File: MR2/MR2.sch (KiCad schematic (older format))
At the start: 12 parts, among them J1 Conn_01x04_Male, J2 Conn_01x04_Male, J3 Conn_01x04_Male, J4 Conn_01x04_Male, J5 Conn_01x02_Male, J6 Conn_01x02_Male, J7 Conn_01x04_Male, J8 Conn_01x02_Male, J9 Conn_01x02_Male, U5 LPC1768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

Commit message: update:MR2の基板完成
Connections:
- net IO_1A: now also J2.2 (Pin_2); no longer J2.3 (Pin_3)
- net IO_1B: now also J2.3 (Pin_3); no longer J2.2 (Pin_2)
- net enc_collect_a: now also J3.2 (Pin_2); no longer J3.3 (Pin_3)
- net enc_collect_b: now also J3.3 (Pin_3); no longer J3.2 (Pin_2)
- net sw1: now also U5.7 (p7)
- net sw2: now also U5.8 (p8)
- net sw3: now also U5.9 (p9)
- no-connect marks 17 -> 23
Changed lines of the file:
@@
 Text GLabel 4300 3200 2    50   Input ~ 0
 PWM_1
+Text GLabel 4300 3400 2    50   Input ~ 0
+IO_1B
 Text GLabel 4300 3300 2    50   Input ~ 0
-IO_1B
-Text GLabel 4300 3400 2    50   Input ~ 0
 IO_1A
 Wire Wire Line
@@
 Text GLabel 5900 2350 2    50   Input ~ 0
 enc_elevator_a
+Text GLabel 5900 3000 2    50   Input ~ 0
+enc_collect_b
 Text GLabel 5900 2900 2    50   Input ~ 0
-enc_collect_b
-Text GLabel 5900 3000 2    50   Input ~ 0
 enc_collect_a
 Wire Notes Line
@@
 	1    0    0    -1
 $EndComp
-NoConn ~ 5300 4300
 Text Label 3350 4850 0    50   ~ 0
 motor
 Text Label 6700 5700 0    50   ~ 0
 switch
+NoConn ~ 5300 4600
+NoConn ~ 5300 4700
+NoConn ~ 5300 4800
+NoConn ~ 5300 4900
+NoConn ~ 6100 5100
+NoConn ~ 6100 5200
+NoConn ~ 4400 2300
+Text GLabel 5300 4300 0    50   Input ~ 0
+sw1
+Text GLabel 5300 4400 0    50   Input ~ 0
+sw2
+Text GLabel 5300 4500 0    50   Input ~ 0
+sw3
 $EndSCHEMATC

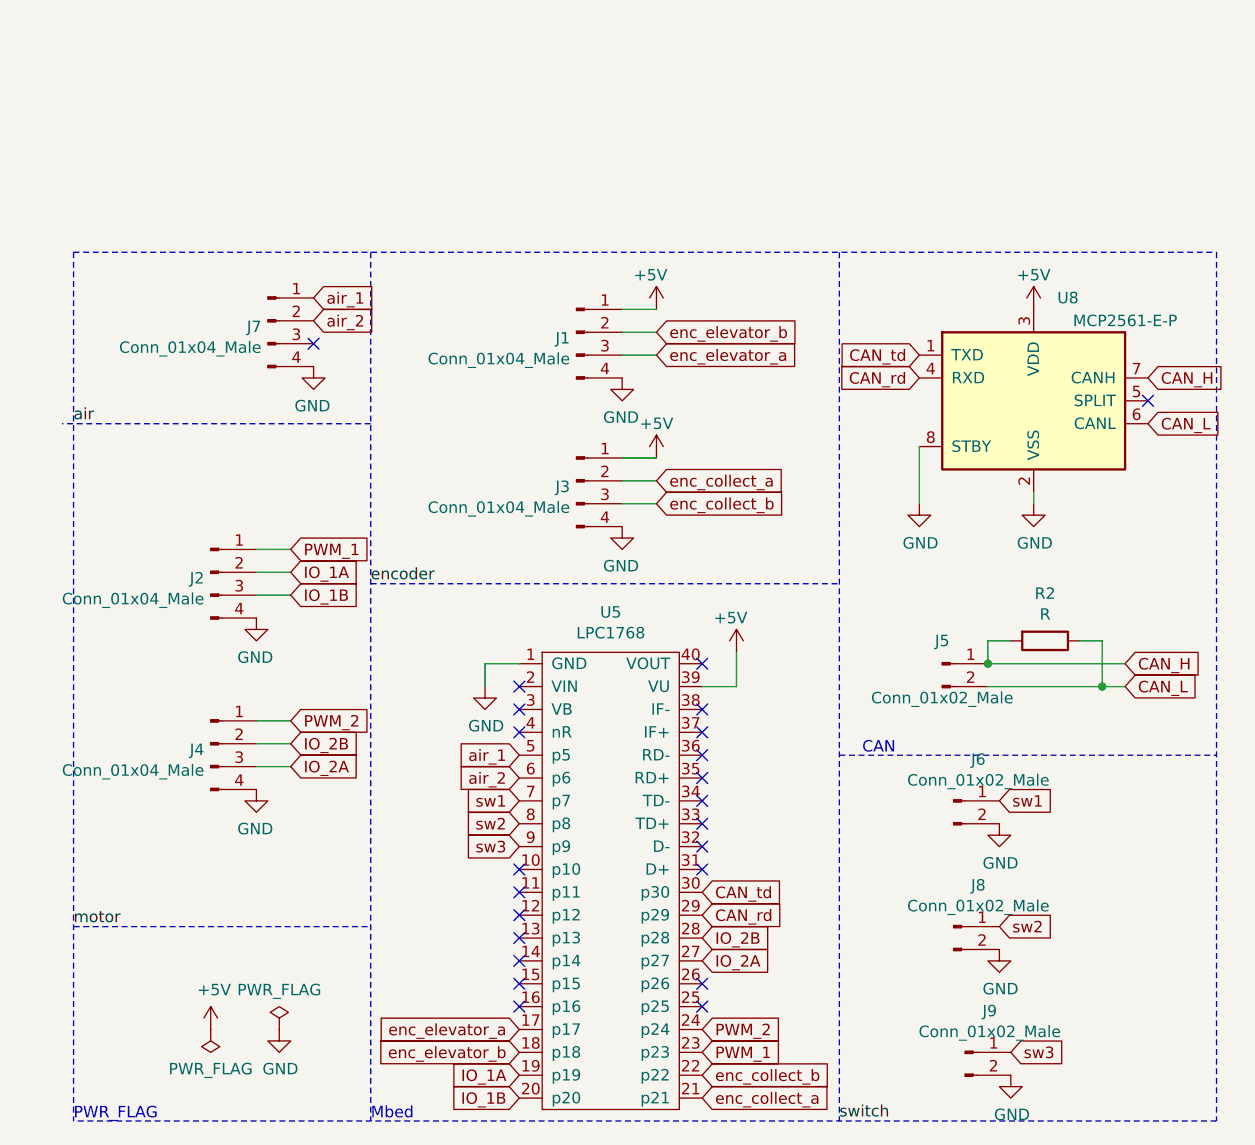
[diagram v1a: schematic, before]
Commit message: update:設計変更に伴う改修、CAN通信周りの不具合を修正
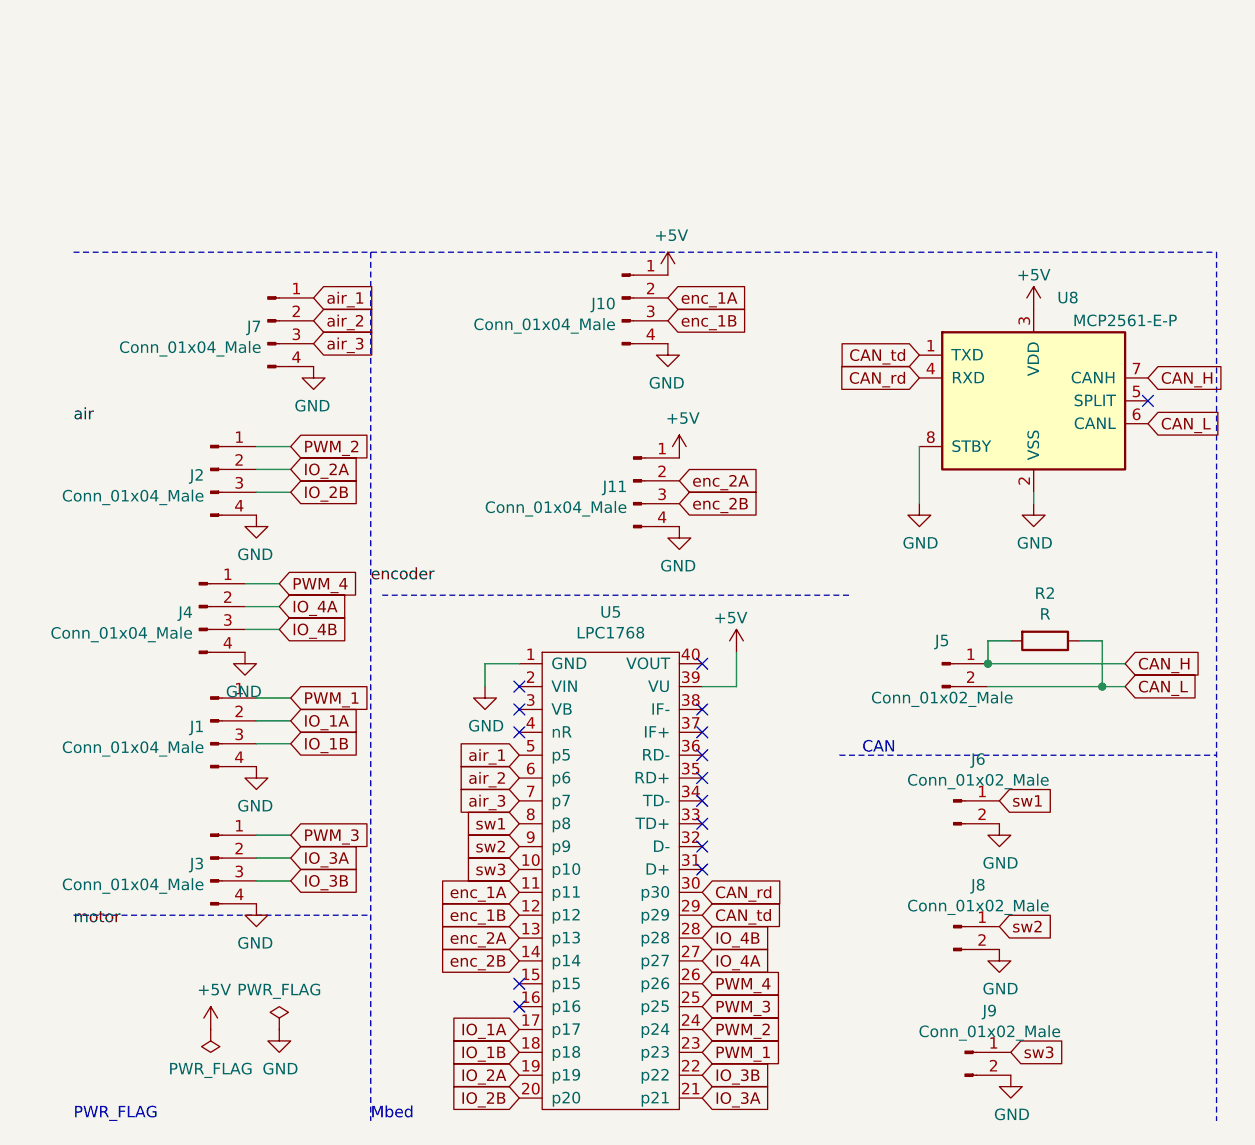
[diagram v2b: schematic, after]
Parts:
- added J10, J11: Conn_01x04_Male, Connector_JST:JST_XH_S4B-XH-A_1x04_P2.50mm_Horizontal, symbol Connector:Conn_01x04_Male
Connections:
- net +5V: now also J10.1 (Pin_1), J11.1 (Pin_1); no longer J1.1 (Pin_1), J3.1 (Pin_1)
- net CAN_rd: now also U5.30 (p30); no longer U5.29 (p29)
- net CAN_td: now also U5.29 (p29); no longer U5.30 (p30)
- net GND: now also J10.4 (Pin_4), J11.4 (Pin_4)
- net IO_1A: now also J1.2 (Pin_2), U5.17 (p17); no longer J2.2 (Pin_2), U5.19 (p19)
- net IO_1B: now also J1.3 (Pin_3), U5.18 (p18); no longer J2.3 (Pin_3), U5.20 (p20)
- net IO_2A: now also J2.2 (Pin_2), U5.19 (p19); no longer J4.3 (Pin_3), U5.27 (p27)
- net IO_2B: now also J2.3 (Pin_3), U5.20 (p20); no longer J4.2 (Pin_2), U5.28 (p28)
- net PWM_1: now also J1.1 (Pin_1); no longer J2.1 (Pin_1)
- net PWM_2: now also J2.1 (Pin_1); no longer J4.1 (Pin_1)
- net sw1: now also U5.8 (p8); no longer U5.7 (p7)
- net sw2: now also U5.9 (p9); no longer U5.8 (p8)
- net sw3: now also U5.10 (p10); no longer U5.9 (p9)
- net enc_1A: now reaches U5.11 (p11)
- net enc_1A: now also J10.2 (Pin_2)
- net enc_1B: now reaches U5.12 (p12)
- net enc_1B: now also J10.3 (Pin_3)
- net enc_2A: now reaches U5.13 (p13)
- net enc_2A: now also J11.2 (Pin_2)
- net enc_2B: now reaches U5.14 (p14)
- net enc_2B: now also J11.3 (Pin_3)
- net PWM_3: now reaches U5.25 (p25)
- net PWM_3: now also J3.1 (Pin_1)
- net PWM_4: now reaches U5.26 (p26)
- net PWM_4: now also J4.1 (Pin_1)
- net air_3: now reaches J7.3 (Pin_3)
- net air_3: now also U5.7 (p7)
- net enc_collect_a renamed IO_3A
- net enc_collect_b renamed IO_3B
- removed net enc_elevator_a: J1.3 (Pin_3), U5.17 (p17)
- removed net enc_elevator_b: J1.2 (Pin_2), U5.18 (p18)
- new net IO_4A: J4.2 (Pin_2), U5.27 (p27)
- new net IO_4B: J4.3 (Pin_3), U5.28 (p28)
- no-connect marks 23 -> 15
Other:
- moved on the sheet: J1, J2, J3, J4

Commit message: update : mr1:sub_swの追加   mr2:エンコーダーの増設
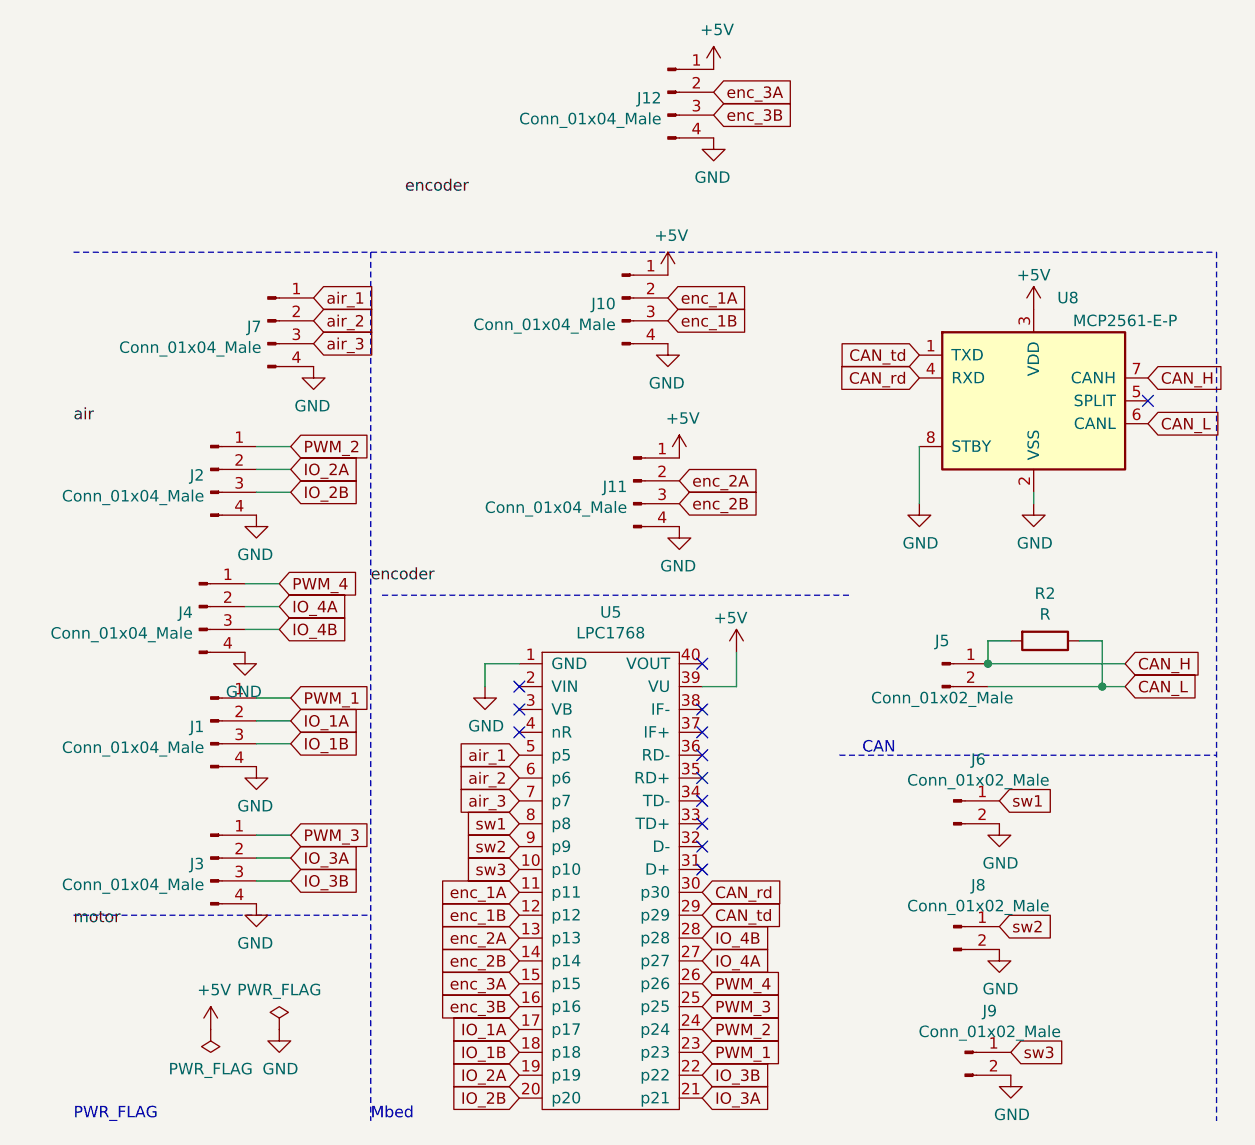
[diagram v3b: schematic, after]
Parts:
- added J12: Conn_01x04_Male, Connector_JST:JST_XH_S4B-XH-A_1x04_P2.50mm_Horizontal, symbol Connector:Conn_01x04_Male
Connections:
- net +5V: now also J12.1 (Pin_1)
- net GND: now also J12.4 (Pin_4)
- net enc_3A: now reaches U5.15 (p15)
- net enc_3A: now also J12.2 (Pin_2)
- net enc_3B: now reaches U5.16 (p16)
- net enc_3B: now also J12.3 (Pin_3)
- no-connect marks 15 -> 13
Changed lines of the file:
@@
 NoConn ~ 6100 4500
 NoConn ~ 6100 4600
-NoConn ~ 5300 5100
-NoConn ~ 5300 5200
 NoConn ~ 5300 3900
 NoConn ~ 5300 4000
@@
 Text GLabel 5300 4300 0    50   Input ~ 0
 air_3
+Text GLabel 5300 5100 0    50   Input ~ 0
+enc_3A
+Text GLabel 5300 5200 0    50   Input ~ 0
+enc_3B
+Text Label 4800 1650 0    50   ~ 0
+encoder
+$Comp
+L power:+5V #PWR017
+U 1 1 5D7B182C
+P 6150 1100
+F 0 "#PWR017" H 6150 950 50  0001 C CNN
+F 1 "+5V" H 6165 1273 50  0000 C CNN
+F 2 "" H 6150 1100 50  0001 C CNN
+F 3 "" H 6150 1100 50  0001 C CNN
+	1    6150 1100
+	1    0    0    -1
+$EndComp
+$Comp
+L power:GND #PWR018
+U 1 1 5D7B1836
+P 6150 1400
+F 0 "#PWR018" H 6150 1150 50  0001 C CNN
+F 1 "GND" H 6155 1227 50  0000 C CNN
+F 2 "" H 6150 1400 50  0001 C CNN
+F 3 "" H 6150 1400 50  0001 C CNN
+	1    6150 1400
+	-1   0    0    -1
+$EndComp
+$Comp
+L Connector:Conn_01x04_Male J12
+U 1 1 5D7B1840
+P 5950 1200
+F 0 "J12" H 5922 1174 50  0000 R CNN
+F 1 "Conn_01x04_Male" H 5922 1083 50  0000 R CNN
+F 2 "Connector_JST:JST_XH_S4B-XH-A_1x04_P2.50mm_Horizontal" H 5950 1200 50  0001 C CNN
+F 3 "~" H 5950 1200 50  0001 C CNN
+	1    5950 1200
+	1    0    0    -1
+$EndComp
+Text GLabel 6150 1200 2    50   Input ~ 0
+enc_3A
+Text GLabel 6150 1300 2    50   Input ~ 0
+enc_3B
 $EndSCHEMATC
